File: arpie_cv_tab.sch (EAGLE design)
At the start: 44 parts, among them IC1 MCP4726, IC2 74HC14D

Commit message: v2 board
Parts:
- added C10, C5: (no value), resistor:C-EUC0805
- added C6: (no value), rcl:CPOL-EUSMCA
- added C7, C8: 10u, rcl:CPOL-EUSMCA
- added D1: MBR0520LT, diode:MBR0520LT
- added IC3: LM27675M5_CHARGEPUMP, jason_eagle6:LM27675M5_CHARGEPUMP
- added IC4: LM358D, linear:LM358D
- added R1, R2, R3, R4, R5: (no value), rcl:R-EU_R0805
- added R13: 1K, rcl:R-EU_R0805
- IC2: value 74HC14D -> MCP601OT; device 74xx-eu:74HC14D -> linear:MCP601OT
- R11, R12, R8: value 10K -> (none)
- R6, R7, R9: value 1K -> (none)
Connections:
- removed net N$13: IC2A.I, R9.2
- removed net N$14: IC2E.I, R6.2
- removed net N$6: GATE_LED.A, R10.2
- removed net N$7: IC1.VOUT, R11.1
- removed net N$8: CLK_LED.A, R7.2
- new net +10V: C10.1, C2.2, C6.+, D1.C, IC2.V+, IC3.OUT, IC4P.V+
- new net CVOUT: CVOUT.T, R1.1, R3.1
- new net DACOUT: IC1.VOUT, IC2.+IN
- new net N$11: C3.2, IC2.OUT, R1.2
- new net N$15: C3.1, IC2.-IN, R2.1, R3.2
- new net N$38: C8.+, IC3.CAP+
- new net N$39: C8.-, IC3.CAP-
- net +5V: now also C1.2, C7.+, D1.A, IC3.V+, R6.2; no longer C1.1, C2.2, IC2P.VCC
- net CLK_OUT: now also CLK_LED.A, R12.2; no longer R9.1
- net GATE_OUT: now also GATE_LED.A, R9.2; no longer R6.1
- net GND: now also C1.1, C10.2, C5.2, C6.-, C7.-, GND1.1, GND2.1, GND3.1, GND4.1, GND5.1, GND6.1, IC2.V-, IC3.GND, IC3.SD, IC4P.V-, R10.2, R13.2, R2.2, R7.1; no longer C1.2, C3.2, CLK_LED.C, GATE_LED.C, IC2P.GND
- net N$1: now also IC4A.-IN, IC4B.-IN, R6.1, R7.2; no longer CVOUT.T, R11.2
- net N$12: now also IC4B.OUT, R4.1, R8.1; no longer IC2F.O, R12.1
- net N$19: now also C5.1, R5.2; no longer C4.1, R8.2
- net N$2: now also CLK_LED.C, R13.1; no longer IC2C.O, R10.1
- net N$20: now also C4.1, R4.2; no longer C3.1, R12.2
- net N$3: now also GATE_LED.C, R10.1; no longer IC2B.O, R7.1
- net N$4: now also IC4A.+IN, R11.2, R12.1; no longer IC2A.O, IC2B.I, IC2D.I
- net N$5: now also IC4B.+IN, R8.2, R9.1; no longer IC2C.I, IC2E.O, IC2F.I
- net N$9: now also IC4A.OUT, R11.1, R5.1; no longer IC2D.O, R8.1
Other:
- note added: "& LEVEL SHIFTER"
- note added: "10V CHARGE PUMP"
- note added: "CC-NC-BY-SA Not to be used for commercial purposes"
- note added: "CV OUT BUFFER (x2 GAIN)"
- note added: "CV TAB FOR ARPIE"
- note added: "DAC"
- note added: "GATE/CLOCK BUFFER"
- note added: "Sixty four pixels limited"
- note added: "VERSION 2 - 17NOV18"
- moved on the sheet: C1, C2, C3, C4, CLK, CLK_LED, DAT, ENA, GATE_LED, GND, GND1, GND2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

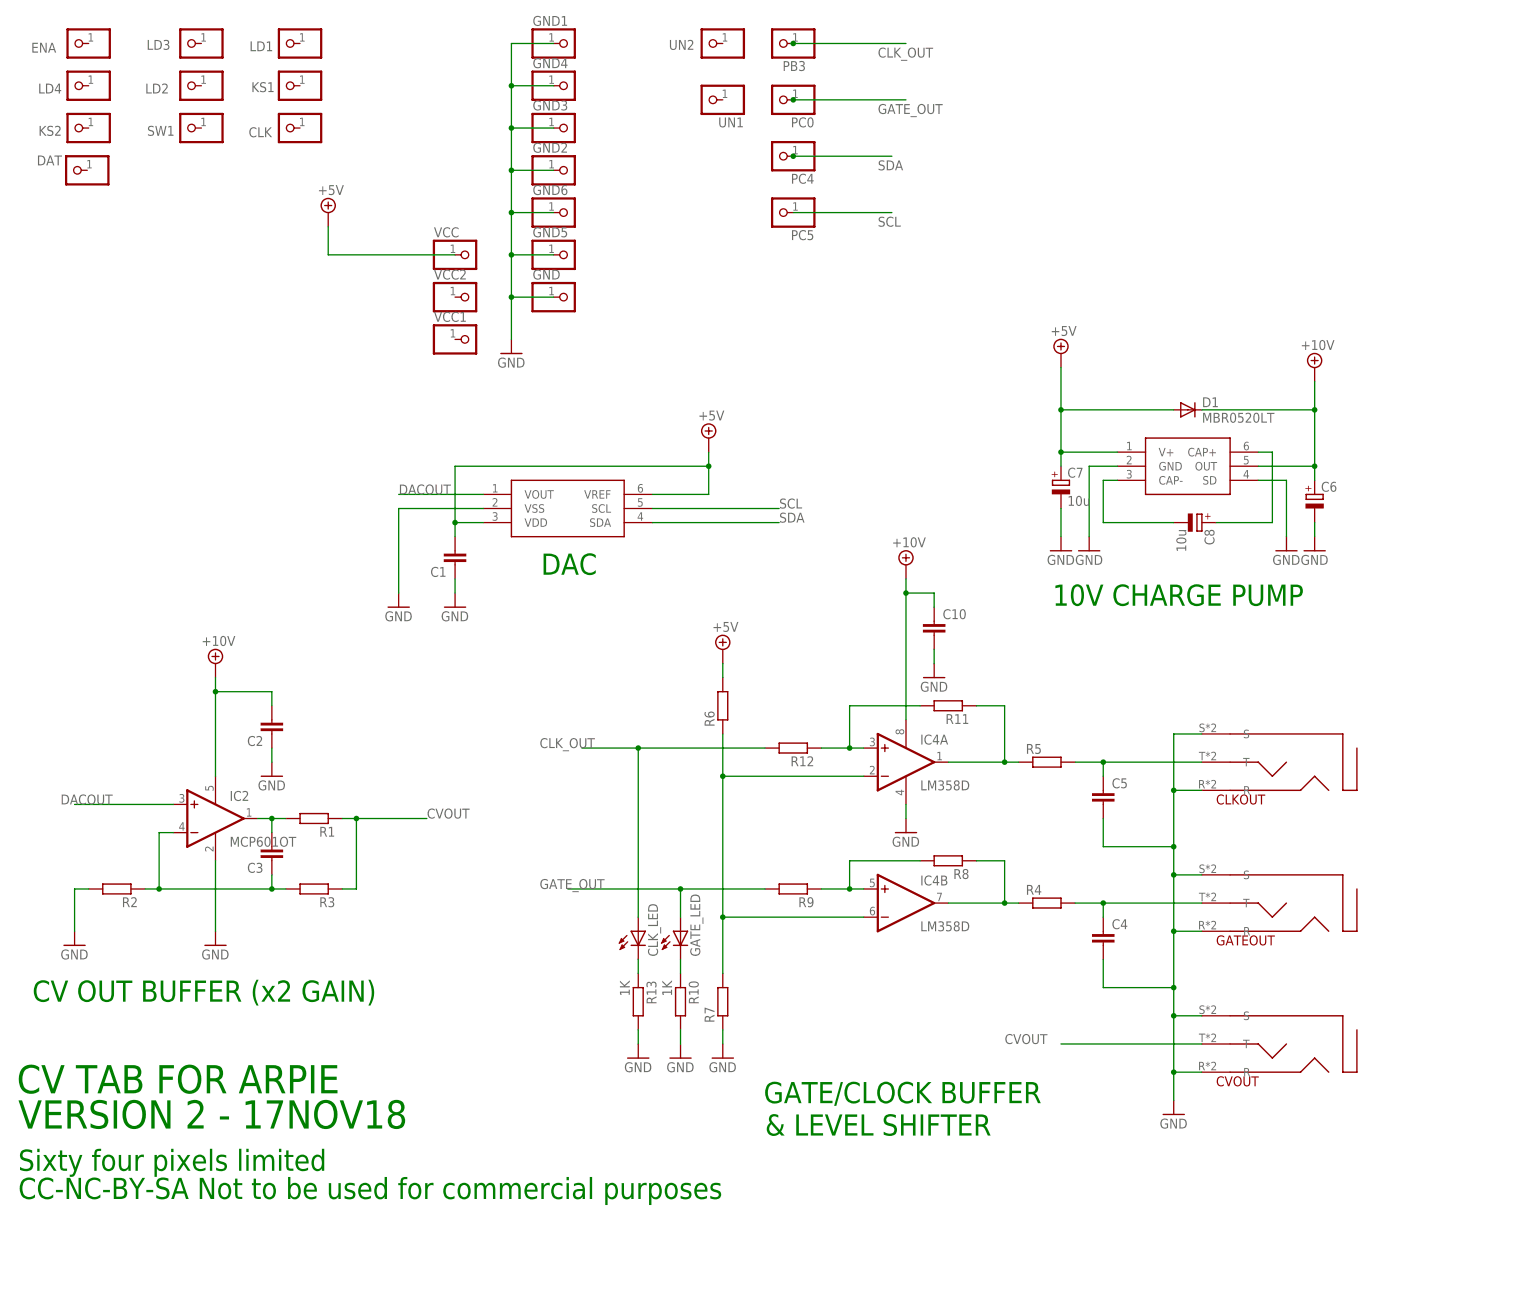
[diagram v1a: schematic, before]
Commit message: v3 board
add voltage reference
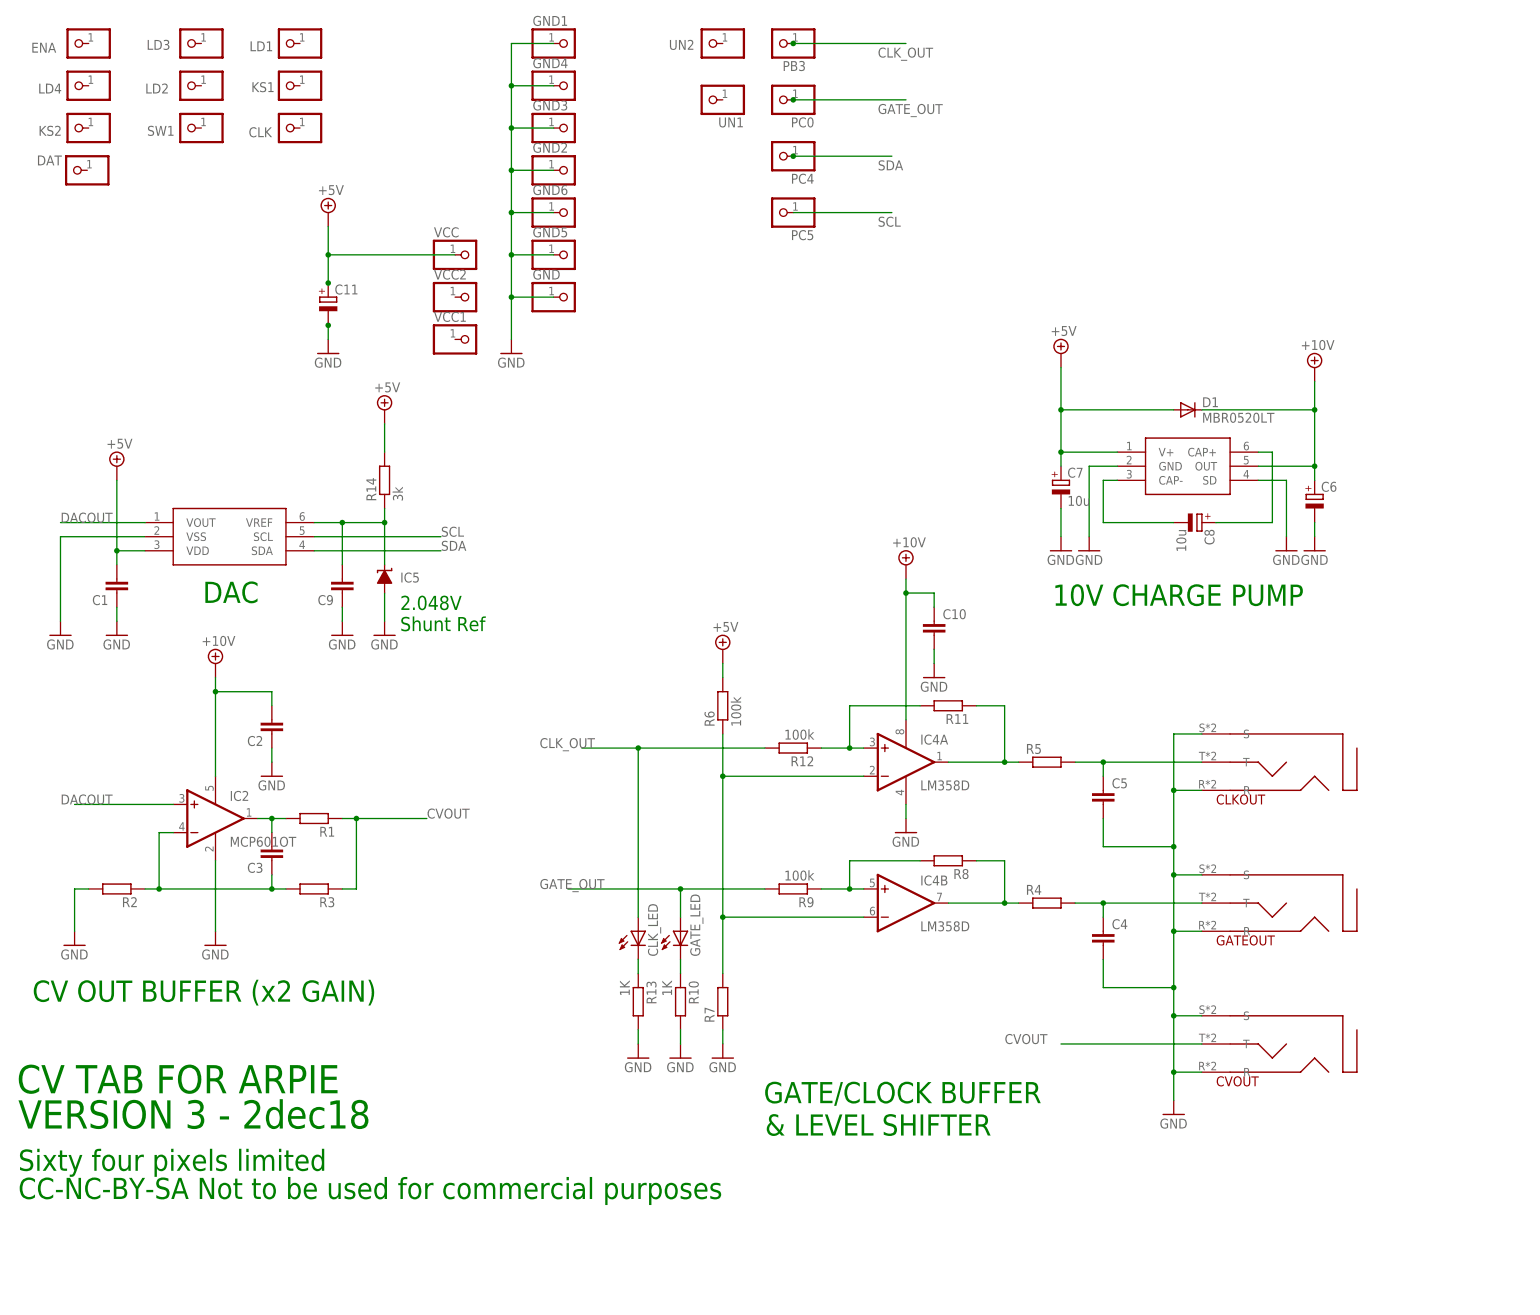
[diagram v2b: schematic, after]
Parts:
- added C11: (no value), rcl:CPOL-EUE2.5-5
- added C9: (no value), resistor:C-EUC0805
- added IC5: LM4041A12DBZ, texas:LM4041A12DBZ
- added R14: 3k, rcl:R-EU_R0805
- R12, R6, R9: value (none) -> 100k
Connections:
- new net N$6: C9.2, IC1.VREF, IC5.C, R14.1
- net +5V: now also C11.+, R14.2; no longer IC1.VREF
- net GND: now also C11.-, C9.1, IC5.A
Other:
- note added: "2.048V Shunt Ref"
- note added: "VERSION 3 - 2dec18"
- note removed: "VERSION 2 - 17NOV18"
- moved on the sheet: C1
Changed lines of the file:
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@@
 <part name="IC4" library="linear" deviceset="LM358" device="D"/>
 <part name="R7" library="rcl" deviceset="R-EU_" device="R0805"/>
-<part name="R6" library="rcl" deviceset="R-EU_" device="R0805"/>
+<part name="R6" library="rcl" deviceset="R-EU_" device="R0805" value="100k"/>
 <part name="GND11" library="SparkFun" deviceset="GND" device=""/>
 <part name="SUPPLY2" library="supply2" deviceset="+5V" device=""/>
@@
 <part name="GND22" library="SparkFun" deviceset="GND" device=""/>
 <part name="SUPPLY8" library="supply2" deviceset="+10V" device=""/>
-<part name="R12" library="rcl" deviceset="R-EU_" device="R0805"/>
-<part name="R9" library="rcl" deviceset="R-EU_" device="R0805"/>
+<part name="R12" library="rcl" deviceset="R-EU_" device="R0805" value="100k"/>
+<part name="R9" library="rcl" deviceset="R-EU_" device="R0805" value="100k"/>
 <part name="R8" library="rcl" deviceset="R-EU_" device="R0805"/>
 <part name="R11" library="rcl" deviceset="R-EU_" device="R0805"/>
 <part name="C10" library="resistor" deviceset="C-EU" device="C0805"/>
+<part name="IC5" library="texas" deviceset="LM4041" device="DBZ" technology="A12"/>
+<part name="R14" library="rcl" deviceset="R-EU_" device="R0805" value="3k"/>
+<part name="SUPPLY3" library="supply2" deviceset="+5V" device=""/>
+<part name="GND23" library="SparkFun" deviceset="GND" device=""/>
+<part name="C9" library="resistor" deviceset="C-EU" device="C0805"/>
+<part name="GND24" library="SparkFun" deviceset="GND" device=""/>
+<part name="GND25" library="SparkFun" deviceset="GND" device=""/>
+<part name="C11" library="rcl" deviceset="CPOL-EU" device="E2.5-5"/>
 </parts>
 <sheets>
@@
 <plain>
 <text x="244.856" y="114.554" size="3.81" layer="91">10V CHARGE PUMP</text>
-<text x="152.654" y="120.142" size="3.81" layer="91">DAC</text>
+<text x="91.694" y="115.062" size="3.81" layer="91">DAC</text>
 <text x="60.96" y="43.18" size="3.81" layer="91">CV OUT BUFFER (x2 GAIN)</text>
 <text x="192.786" y="24.892" size="3.81" layer="91">GATE/CLOCK BUFFER</text>
 <text x="193.04" y="19.05" size="3.81" layer="91">&amp; LEVEL SHIFTER</text>
 <text x="58.166" y="26.67" size="5.08" layer="91">CV TAB FOR ARPIE</text>
-<text x="58.42" y="20.32" size="5.08" layer="91">VERSION 2 - 17NOV18</text>
+<text x="58.42" y="20.32" size="5.08" layer="91">VERSION 3 - 2dec18</text>
 <text x="58.42" y="12.7" size="3.81" layer="91">Sixty four pixels limited</text>
 <text x="58.42" y="7.62" size="3.81" layer="91">CC-NC-BY-SA Not to be used for commercial purposes</text>
+<text x="127.254" y="109.982" size="2.54" layer="91">2.048V
+Shunt Ref</text>
 </plain>
 <instances>
@@
 <instance part="GATEOUT" gate="G$1" x="276.86" y="60.96" rot="R270"/>
 <instance part="CVOUT" gate="G$1" x="276.86" y="35.56" rot="R270"/>
-<instance part="IC1" gate="G$1" x="157.48" y="132.08"/>
+<instance part="IC1" gate="G$1" x="96.52" y="127"/>
 <instance part="C5" gate="G$1" x="254" y="81.28"/>
 <instance part="C4" gate="G$1" x="254" y="55.88"/>
@@
 <instance part="GND16" gate="1" x="266.7" y="22.86"/>
 <instance part="R4" gate="G$1" x="243.84" y="60.96"/>
-<instance part="SUPPLY1" gate="+5V" x="182.88" y="144.78"/>
-<instance part="GND7" gate="1" x="127" y="114.3"/>
-<instance part="C1" gate="G$1" x="137.16" y="121.92" rot="R180"/>
-<instance part="GND9" gate="1" x="137.16" y="114.3"/>
+<instance part="SUPPLY1" gate="+5V" x="76.2" y="139.7"/>
+<instance part="GND7" gate="1" x="66.04" y="109.22"/>
+<instance part="C1" gate="G$1" x="76.2" y="116.84" rot="R180"/>
+<instance part="GND9" gate="1" x="76.2" y="109.22"/>
 <instance part="IC2" gate="G$1" x="93.98" y="76.2"/>
 <instance part="R1" gate="G$1" x="111.76" y="76.2" rot="R180"/>
@@
 <instance part="R11" gate="G$1" x="226.06" y="96.52" rot="R180"/>
 <instance part="C10" gate="G$1" x="223.52" y="111.76"/>
+<instance part="IC5" gate="G$1" x="124.46" y="119.38" smashed="yes">
+<attribute name="NAME" x="127.254" y="118.745" size="1.778" layer="95"/>
+</instance>
+<instance part="R14" gate="G$1" x="124.46" y="137.16" rot="R90"/>
+<instance part="SUPPLY3" gate="+5V" x="124.46" y="149.86"/>
+<instance part="GND23" gate="1" x="124.46" y="109.22"/>
+<instance part="C9" gate="G$1" x="116.84" y="116.84" rot="R180"/>
+<instance part="GND24" gate="1" x="116.84" y="109.22"/>
+<instance part="GND25" gate="1" x="114.3" y="160.02"/>
+<instance part="C11" gate="G$1" x="114.3" y="170.18"/>
 </instances>
 <busses>
@@
 <pinref part="IC1" gate="G$1" pin="VSS"/>
 <pinref part="GND7" gate="1" pin="GND"/>
-<wire x1="142.24" y1="132.08" x2="127" y2="132.08" width="0.1524" layer="91"/>
-<wire x1="127" y1="132.08" x2="127" y2="116.84" width="0.1524" layer="91"/>
+<wire x1="81.28" y1="127" x2="66.04" y2="127" width="0.1524" layer="91"/>
+<wire x1="66.04" y1="127" x2="66.04" y2="111.76" width="0.1524" layer="91"/>
 </segment>
 <segment>
 <pinref part="GND9" gate="1" pin="GND"/>
 <pinref part="C1" gate="G$1" pin="1"/>
-<wire x1="137.16" y1="116.84" x2="137.16" y2="119.38" width="0.1524" layer="91"/>
+<wire x1="76.2" y1="111.76" x2="76.2" y2="114.3" width="0.1524" layer="91"/>
 </segment>
 <segment>
@@
 <wire x1="223.52" y1="104.14" x2="223.52" y2="106.68" width="0.1524" layer="91"/>
 </segment>
+<segment>
+<pinref part="GND23" gate="1" pin="GND"/>
+<pinref part="IC5" gate="G$1" pin="A"/>
+<wire x1="124.46" y1="111.76" x2="124.46" y2="116.84" width="0.1524" layer="91"/>
+</segment>
+<segment>
+<pinref part="GND24" gate="1" pin="GND"/>
+<pinref part="C9" gate="G$1" pin="1"/>
+<wire x1="116.84" y1="111.76" x2="116.84" y2="114.3" width="0.1524" layer="91"/>
+</segment>
+<segment>
+<pinref part="GND25" gate="1" pin="GND"/>
+<wire x1="114.3" y1="162.56" x2="114.3" y2="165.1" width="0.1524" layer="91"/>
+<pinref part="C11" gate="G$1" pin="-"/>
+<junction x="114.3" y="165.1"/>
+</segment>
 </net>
 <net name="+5V" class="0">
@@
 <wire x1="114.3" y1="177.8" x2="114.3" y2="182.88" width="0.1524" layer="91"/>
 <pinref part="SUPPLY4" gate="+5V" pin="+5V"/>
+<wire x1="114.3" y1="172.72" x2="114.3" y2="177.8" width="0.1524" layer="91"/>
+<junction x="114.3" y="177.8"/>
+<pinref part="C11" gate="G$1" pin="+"/>
+<junction x="114.3" y="172.72"/>
 </segment>
 <segment>
 <pinref part="IC1" gate="G$1" pin="VDD"/>
-<wire x1="142.24" y1="129.54" x2="137.16" y2="129.54" width="0.1524" layer="91"/>
-<wire x1="137.16" y1="129.54" x2="137.16" y2="139.7" width="0.1524" layer="91"/>
+<wire x1="81.28" y1="124.46" x2="76.2" y2="124.46" width="0.1524" layer="91"/>
+<wire x1="76.2" y1="124.46" x2="76.2" y2="137.16" width="0.1524" layer="91"/>
 <pinref part="SUPPLY1" gate="+5V" pin="+5V"/>
-<wire x1="137.16" y1="139.7" x2="182.88" y2="139.7" width="0.1524" layer="91"/>
-<wire x1="182.88" y1="139.7" x2="182.88" y2="142.24" width="0.1524" layer="91"/>
-<pinref part="IC1" gate="G$1" pin="VREF"/>
-<wire x1="172.72" y1="134.62" x2="182.88" y2="134.62" width="0.1524" layer="91"/>
-<wire x1="182.88" y1="134.62" x2="182.88" y2="139.7" width="0.1524" layer="91"/>
-<junction x="182.88" y="139.7"/>
 <pinref part="C1" gate="G$1" pin="2"/>
-<wire x1="137.16" y1="127" x2="137.16" y2="129.54" width="0.1524" layer="91"/>
-<junction x="137.16" y="129.54"/>
+<wire x1="76.2" y1="121.92" x2="76.2" y2="124.46" width="0.1524" layer="91"/>
+<junction x="76.2" y="124.46"/>
 </segment>
 <segment>
@@
 <wire x1="185.42" y1="101.6" x2="185.42" y2="104.14" width="0.1524" layer="91"/>
 </segment>
+<segment>
+<pinref part="R14" gate="G$1" pin="2"/>
+<pinref part="SUPPLY3" gate="+5V" pin="+5V"/>
+<wire x1="124.46" y1="142.24" x2="124.46" y2="147.32" width="0.1524" layer="91"/>
+</segment>
 </net>
 <net name="CLK_OUT" class="0">
@@
 <segment>
 <pinref part="IC1" gate="G$1" pin="SCL"/>
-<wire x1="172.72" y1="132.08" x2="195.58" y2="132.08" width="0.1524" layer="91"/>
-<label x="195.58" y="132.08" size="1.778" layer="95"/>
+<wire x1="111.76" y1="127" x2="134.62" y2="127" width="0.1524" layer="91"/>
+<label x="134.62" y="127" size="1.778" layer="95"/>
 </segment>
 <segment>
@@
 <segment>
 <pinref part="IC1" gate="G$1" pin="SDA"/>
-<wire x1="172.72" y1="129.54" x2="195.58" y2="129.54" width="0.1524" layer="91"/>
-<label x="195.58" y="129.54" size="1.778" layer="95"/>
+<wire x1="111.76" y1="124.46" x2="134.62" y2="124.46" width="0.1524" layer="91"/>
+<label x="134.62" y="124.46" size="1.778" layer="95"/>
 </segment>
 <segment>
@@
 <segment>
 <pinref part="IC1" gate="G$1" pin="VOUT"/>
-<wire x1="142.24" y1="134.62" x2="127" y2="134.62" width="0.1524" layer="91"/>
-<label x="127" y="134.62" size="1.778" layer="95"/>
+<wire x1="81.28" y1="129.54" x2="66.04" y2="129.54" width="0.1524" layer="91"/>
+<label x="66.04" y="129.54" size="1.778" layer="95"/>
 </segment>
 </net>
@@
 </segment>
 </net>
+<net name="N$6" class="0">
+<segment>
+<pinref part="IC1" gate="G$1" pin="VREF"/>
+<wire x1="111.76" y1="129.54" x2="116.84" y2="129.54" width="0.1524" layer="91"/>
+<pinref part="R14" gate="G$1" pin="1"/>
+<wire x1="116.84" y1="129.54" x2="124.46" y2="129.54" width="0.1524" layer="91"/>
+<wire x1="124.46" y1="132.08" x2="124.46" y2="129.54" width="0.1524" layer="91"/>
+<pinref part="IC5" gate="G$1" pin="C"/>
+<wire x1="124.46" y1="121.92" x2="124.46" y2="129.54" width="0.1524" layer="91"/>
+<junction x="124.46" y="129.54"/>
+<pinref part="C9" gate="G$1" pin="2"/>
+<wire x1="116.84" y1="121.92" x2="116.84" y2="129.54" width="0.1524" layer="91"/>
+<junction x="116.84" y="129.54"/>
+</segment>
+</net>
 </nets>
 </sheet>
@@
 </schematic>
 </drawing>
+<compatibility>
+<note version="6.3" minversion="6.2.2" severity="warning">
+Since Version 6.2.2 text objects can contain more than one line,
+which will not be processed correctly with this version.
+</note>
+</compatibility>
 </eagle>
